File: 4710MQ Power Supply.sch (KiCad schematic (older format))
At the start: 24 parts, among them J1 Jack-DC, J2 ATX 4 Pin, J3 Molex 4 Pin, U1 MP1499GD-Z

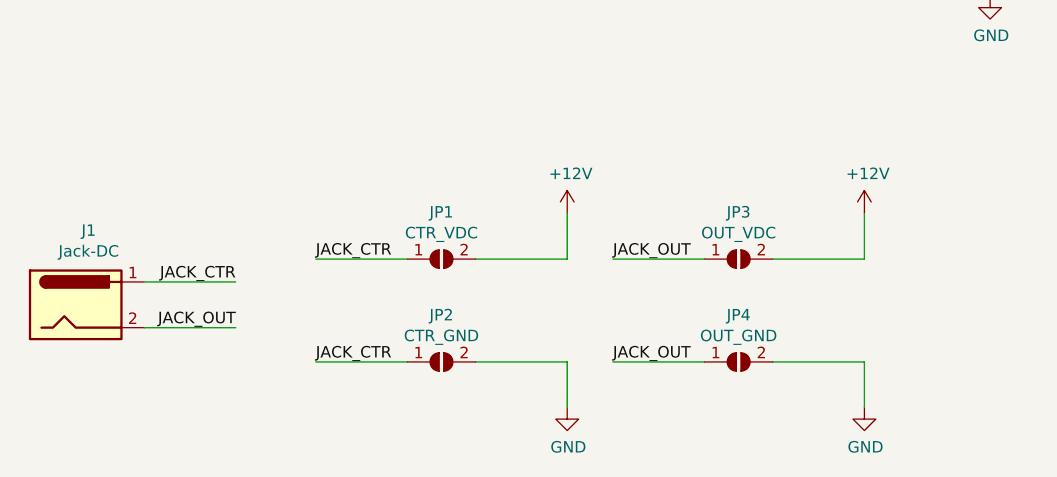
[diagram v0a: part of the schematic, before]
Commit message: Version 1.1
- Add DC-015 (Vertical DC Jack)
- Removed Jumpers (Innerside - +12V / Outside - GND fixed)
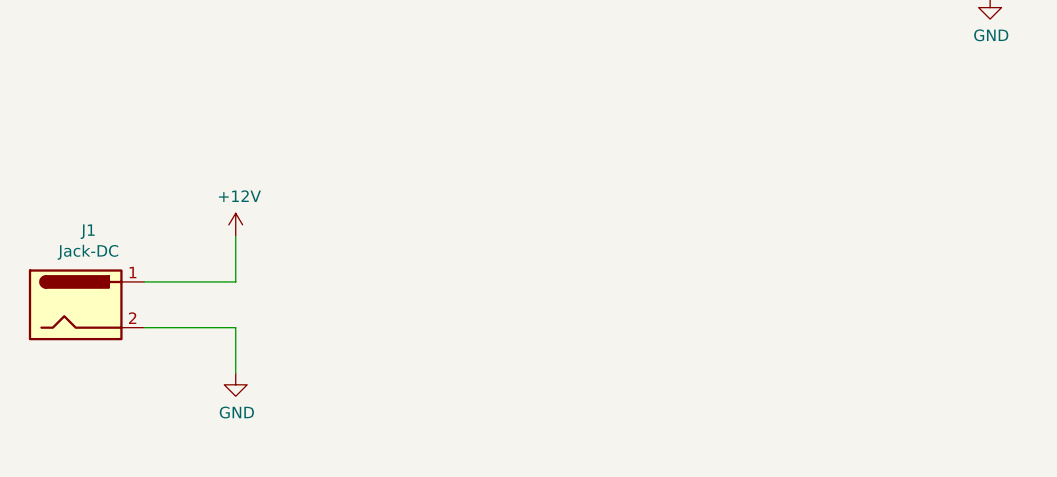
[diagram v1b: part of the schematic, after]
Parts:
- removed JP1: CTR_VDC, Jumper:SolderJumper-3_P1.3mm_Open_Pad1.0x1.5mm_NumberLabels, symbol Jumper:SolderJumper_2_Open
- removed JP2: CTR_GND, Jumper:SolderJumper-3_P1.3mm_Open_Pad1.0x1.5mm_NumberLabels, symbol Jumper:SolderJumper_2_Open
- removed JP3: OUT_VDC, Jumper:SolderJumper-3_P1.3mm_Open_Pad1.0x1.5mm_NumberLabels, symbol Jumper:SolderJumper_2_Open
- removed JP4: OUT_GND, Jumper:SolderJumper-3_P1.3mm_Open_Pad1.0x1.5mm_NumberLabels, symbol Jumper:SolderJumper_2_Open
- J1: footprint Connector_BarrelJack:BarrelJack_CUI_PJ-063AH_Horizontal -> DC015:DC015
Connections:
- net JACK_CTR is gone; now on net +12V: J1.1
- net JACK_OUT is gone; now on net GND: J1.2
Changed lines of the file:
@@
 F 0 "J1" H 907 5425 50  0000 C CNN
 F 1 "Jack-DC" H 907 5334 50  0000 C CNN
-F 2 "Connector_BarrelJack:BarrelJack_CUI_PJ-063AH_Horizontal" H 900 5060 50  0001 C CNN
+F 2 "DC015:DC015" H 900 5060 50  0001 C CNN
 F 3 "~" H 900 5060 50  0001 C CNN
 	1    850  5100
@@
 Wire Wire Line
 	1150 5200 1550 5200
-Text Label 1550 5000 2    50   ~ 0
-JACK_CTR
-Text Label 1550 5200 2    50   ~ 0
-JACK_OUT
-$Comp
-L Jumper:SolderJumper_2_Open JP1
-U 1 1 611D7CEA
-P 2450 4900
-F 0 "JP1" H 2450 5105 50  0000 C CNN
-F 1 "CTR_VDC" H 2450 5014 50  0000 C CNN
-F 2 "Jumper:SolderJumper-3_P1.3mm_Open_Pad1.0x1.5mm_NumberLabels" H 2450 4900 50  0001 C CNN
-F 3 "~" H 2450 4900 50  0001 C CNN
-	1    2450 4900
-	1    0    0    -1
-$EndComp
-Wire Wire Line
-	2300 4900 1900 4900
-Wire Wire Line
-	2600 4900 3000 4900
-Wire Wire Line
-	3000 4900 3000 4700
-$Comp
-L Jumper:SolderJumper_2_Open JP3
-U 1 1 611E0BFC
-P 3750 4900
-F 0 "JP3" H 3750 5105 50  0000 C CNN
-F 1 "OUT_VDC" H 3750 5014 50  0000 C CNN
-F 2 "Jumper:SolderJumper-3_P1.3mm_Open_Pad1.0x1.5mm_NumberLabels" H 3750 4900 50  0001 C CNN
-F 3 "~" H 3750 4900 50  0001 C CNN
-	1    3750 4900
-	1    0    0    -1
-$EndComp
-Wire Wire Line
-	3600 4900 3200 4900
-Wire Wire Line
-	3900 4900 4300 4900
-Wire Wire Line
-	4300 4900 4300 4700
-$Comp
-L Jumper:SolderJumper_2_Open JP2
-U 1 1 611E1F90
-P 2450 5350
-F 0 "JP2" H 2450 5555 50  0000 C CNN
-F 1 "CTR_GND" H 2450 5464 50  0000 C CNN
-F 2 "Jumper:SolderJumper-3_P1.3mm_Open_Pad1.0x1.5mm_NumberLabels" H 2450 5350 50  0001 C CNN
-F 3 "~" H 2450 5350 50  0001 C CNN
-	1    2450 5350
-	1    0    0    -1
-$EndComp
-Wire Wire Line
-	2300 5350 1900 5350
-Wire Wire Line
-	2600 5350 3000 5350
-$Comp
-L Jumper:SolderJumper_2_Open JP4
-U 1 1 611E3280
-P 3750 5350
-F 0 "JP4" H 3750 5555 50  0000 C CNN
-F 1 "OUT_GND" H 3750 5464 50  0000 C CNN
-F 2 "Jumper:SolderJumper-3_P1.3mm_Open_Pad1.0x1.5mm_NumberLabels" H 3750 5350 50  0001 C CNN
-F 3 "~" H 3750 5350 50  0001 C CNN
-	1    3750 5350
-	1    0    0    -1
-$EndComp
-Wire Wire Line
-	3600 5350 3200 5350
-Wire Wire Line
-	3900 5350 4300 5350
-Wire Wire Line
-	3000 5350 3000 5550
-Wire Wire Line
-	4300 5350 4300 5550
-$Comp
-L power:GND #PWR0109
-U 1 1 611E7F6F
-P 3000 5550
-F 0 "#PWR0109" H 3000 5300 50  0001 C CNN
-F 1 "GND" H 3005 5377 50  0000 C CNN
-F 2 "" H 3000 5550 50  0001 C CNN
-F 3 "" H 3000 5550 50  0001 C CNN
-	1    3000 5550
-	1    0    0    -1
-$EndComp
-$Comp
-L power:GND #PWR0110
-U 1 1 611E86F6
-P 4300 5550
-F 0 "#PWR0110" H 4300 5300 50  0001 C CNN
-F 1 "GND" H 4305 5377 50  0000 C CNN
-F 2 "" H 4300 5550 50  0001 C CNN
-F 3 "" H 4300 5550 50  0001 C CNN
-	1    4300 5550
-	1    0    0    -1
-$EndComp
-Text Label 1900 4900 0    50   ~ 0
-JACK_CTR
-Text Label 1900 5350 0    50   ~ 0
-JACK_CTR
-Text Label 3200 4900 0    50   ~ 0
-JACK_OUT
-Text Label 3200 5350 0    50   ~ 0
-JACK_OUT
 Wire Wire Line
 	700  1200 700  1000
@@
 F 3 "" H 6800 1400 50  0001 C CNN
 	1    6800 1400
-	1    0    0    -1
-$EndComp
-$Comp
-L power:+12V #PWR0112
-U 1 1 61204452
-P 4300 4700
-F 0 "#PWR0112" H 4300 4550 50  0001 C CNN
-F 1 "+12V" H 4315 4873 50  0000 C CNN
-F 2 "" H 4300 4700 50  0001 C CNN
-F 3 "" H 4300 4700 50  0001 C CNN
-	1    4300 4700
-	1    0    0    -1
-$EndComp
-$Comp
-L power:+12V #PWR0113
-U 1 1 61204D4E
-P 3000 4700
-F 0 "#PWR0113" H 3000 4550 50  0001 C CNN
-F 1 "+12V" H 3015 4873 50  0000 C CNN
-F 2 "" H 3000 4700 50  0001 C CNN
-F 3 "" H 3000 4700 50  0001 C CNN
-	1    3000 4700
 	1    0    0    -1
 $EndComp
@@
 Wire Wire Line
 	1350 1200 1950 1200
+Wire Wire Line
+	1550 5000 1550 4800
+Wire Wire Line
+	1550 5200 1550 5400
+$Comp
+L power:+12V #PWR0109
+U 1 1 61356D30
+P 1550 4800
+F 0 "#PWR0109" H 1550 4650 50  0001 C CNN
+F 1 "+12V" H 1565 4973 50  0000 C CNN
+F 2 "" H 1550 4800 50  0001 C CNN
+F 3 "" H 1550 4800 50  0001 C CNN
+	1    1550 4800
+	1    0    0    -1
+$EndComp
+$Comp
+L power:GND #PWR0110
+U 1 1 6135740B
+P 1550 5400
+F 0 "#PWR0110" H 1550 5150 50  0001 C CNN
+F 1 "GND" H 1555 5227 50  0000 C CNN
+F 2 "" H 1550 5400 50  0001 C CNN
+F 3 "" H 1550 5400 50  0001 C CNN
+	1    1550 5400
+	1    0    0    -1
+$EndComp
 $EndSCHEMATC

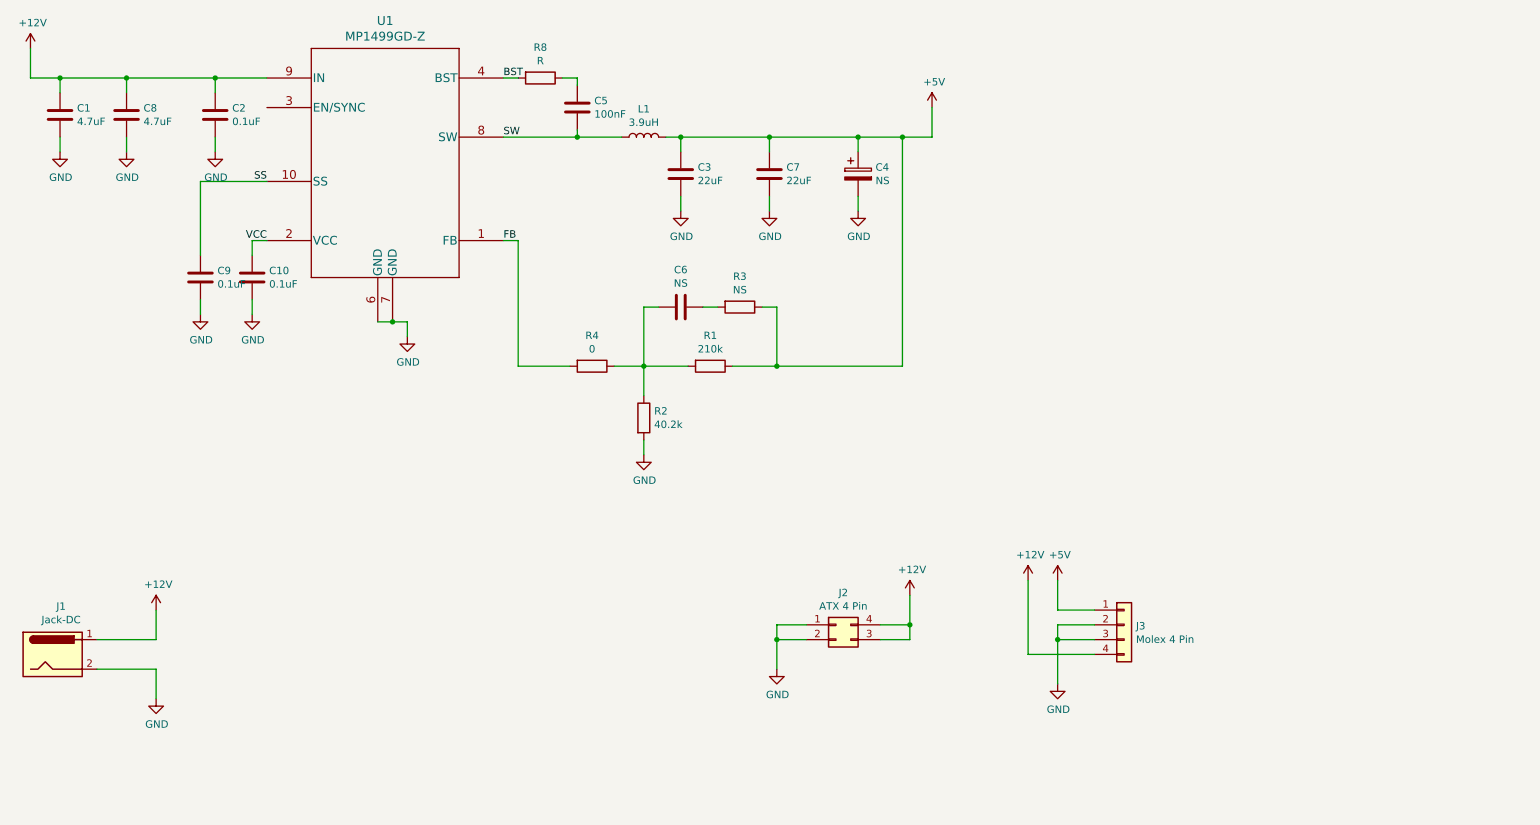
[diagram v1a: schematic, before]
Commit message: [Not Completed] Version 1.2
- 3.3V LDO
- Current Sensor up to 30A
- UART to USB (CH340G)
- ADC 12bit
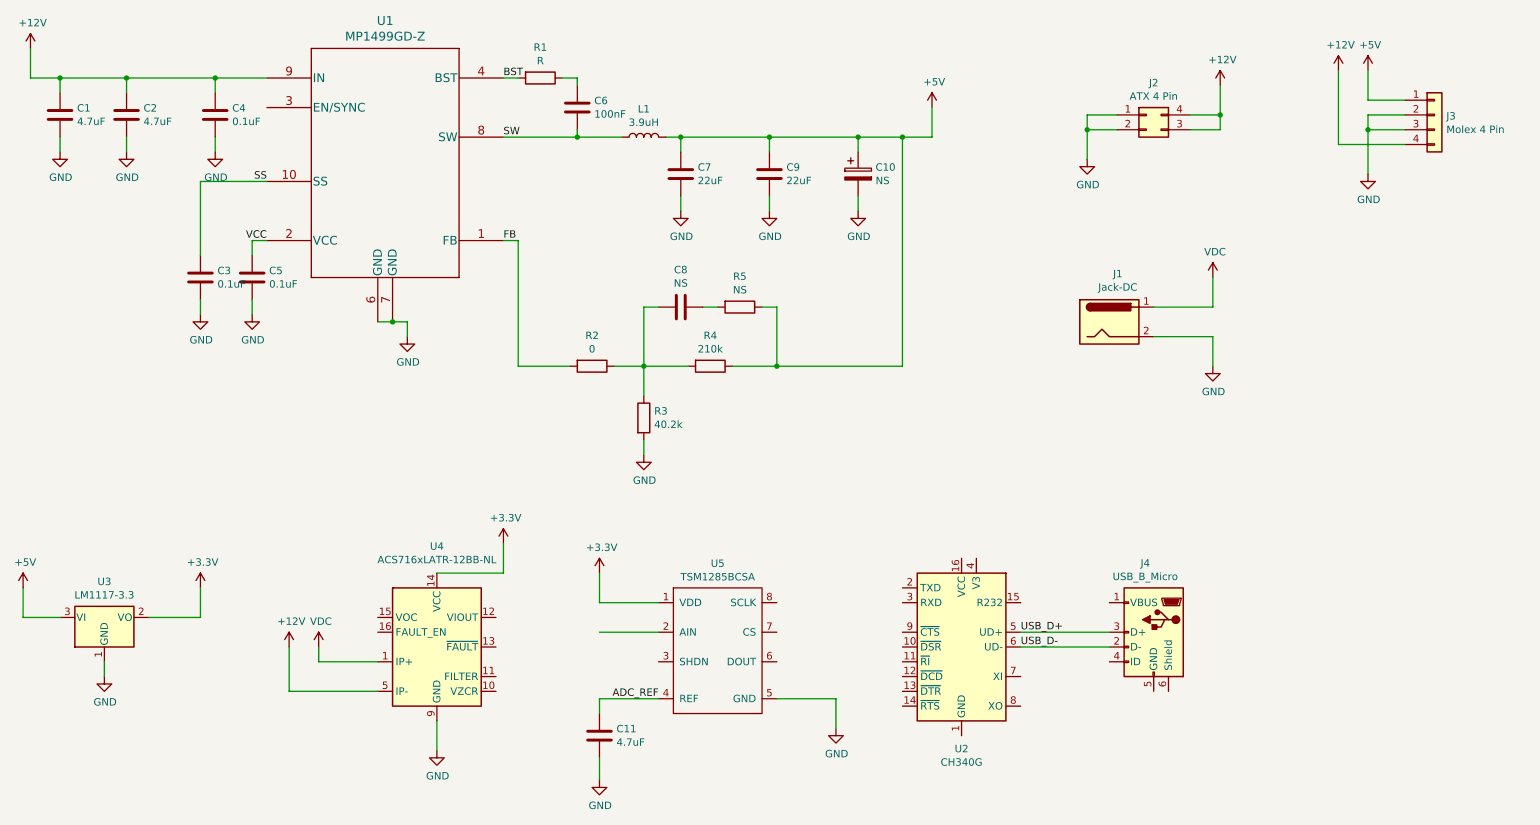
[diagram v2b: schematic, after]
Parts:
- added C11: 4.7uF, Capacitor_SMD:C_1206_3216Metric_Pad1.33x1.80mm_HandSolder, symbol Device:C
- added J4: USB_B_Micro, Connector_USB:USB_Micro-B_Wuerth_614105150721_Vertical, symbol Connector:USB_B_Micro
- added U2: CH340G, Package_SO:SOIC-16_3.9x9.9mm_P1.27mm, symbol Interface_USB:CH340G
- added U3: LM1117-3.3, Package_TO_SOT_SMD:SOT-23_Handsoldering, symbol Regulator_Linear:LM1117-3.3
- added U4: ACS716xLATR-12BB-NL, Package_SO:SOIC-16W_7.5x10.3mm_P1.27mm, symbol Sensor_Current:ACS716xLATR-12BB-NL
- added U5: TSM1285BCSA, Package_SO:SOIC-8_3.9x4.9mm_P1.27mm, symbol TSM1285BCSA:TSM1285BCSA
- renumbered C4 to C10, C8 to C2, C9 to C3, C2 to C4, C10 to C5, C5 to C6, C3 to C7, C6 to C8, C7 to C9, R8 to R1, R4 to R2, R2 to R3, R1 to R4, R3 to R5
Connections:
- net +12V: now also U4.5 (IP-), U4.6 (IP-), U4.7 (IP-), U4.8 (IP-); no longer J1.1
- net +5V: now also U3.3 (VI)
- net GND: now also C11.2, U3.1 (GND), U4.9 (GND), U5.5 (GND)
- new net +3V3: U3.2 (VO), U4.14 (VCC), U5.1 (VDD)
- new net ADC_REF: C11.1, U5.4 (REF)
- new net USB_D+: J4.3 (D+), U2.5 (UD+)
- new net USB_D-: J4.2 (D-), U2.6 (UD-)
- new net VDC: J1.1, U4.1 (IP+), U4.2 (IP+), U4.3 (IP+), U4.4 (IP+)
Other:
- moved on the sheet: J1, J2, J3

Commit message: Version 2.0
- Size Changed
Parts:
- removed C11: 4.7uF, Capacitor_SMD:C_1206_3216Metric_Pad1.33x1.80mm_HandSolder, symbol Device:C
- removed J4: USB_B_Micro, Connector_USB:USB_Micro-B_Wuerth_614105150721_Vertical, symbol Connector:USB_B_Micro
- removed U2: CH340G, Package_SO:SOIC-16_3.9x9.9mm_P1.27mm, symbol Interface_USB:CH340G
- removed U3: LM1117-3.3, Package_TO_SOT_SMD:SOT-23_Handsoldering, symbol Regulator_Linear:LM1117-3.3
- removed U4: ACS716xLATR-12BB-NL, Package_SO:SOIC-16W_7.5x10.3mm_P1.27mm, symbol Sensor_Current:ACS716xLATR-12BB-NL
- removed U5: TSM1285BCSA, Package_SO:SOIC-8_3.9x4.9mm_P1.27mm, symbol TSM1285BCSA:TSM1285BCSA
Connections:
- net VDC is gone; now on net +12V: J1.1
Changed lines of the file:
@@
 Wire Wire Line
 	4850 3650 4850 3750
-$Comp
-L power:GND #PWR010
-U 1 1 611AF7F5
-P 4850 3750
-F 0 "#PWR010" H 4850 3500 50  0001 C CNN
-F 1 "GND" H 4855 3577 50  0000 C CNN
-F 2 "" H 4850 3750 50  0001 C CNN
-F 3 "" H 4850 3750 50  0001 C CNN
-	1    4850 3750
-	1    0    0    -1
-$EndComp
 Wire Wire Line
 	4000 3150 4350 3150
@@
 $EndComp
 $Comp
-L power:VDC #PWR0112
-U 1 1 613D046F
+L power:+12V #PWR0101
+U 1 1 614C8ABC
 P 8700 2550
-F 0 "#PWR0112" H 8700 2450 50  0001 C CNN
-F 1 "VDC" H 8715 2723 50  0000 C CNN
+F 0 "#PWR0101" H 8700 2400 50  0001 C CNN
+F 1 "+12V" H 8715 2723 50  0000 C CNN
 F 2 "" H 8700 2550 50  0001 C CNN
 F 3 "" H 8700 2550 50  0001 C CNN
@@
 	1    0    0    -1
 $EndComp
-Text Label 4950 5400 2    50   ~ 0
-ADC_REF
-Text Label 7400 5050 0    50   ~ 0
-USB_D-
-Text Label 7400 4950 0    50   ~ 0
-USB_D+
-Wire Wire Line
-	7400 5050 8000 5050
-Wire Wire Line
-	7400 4950 8000 4950
-$Comp
-L power:GND #PWR0108
-U 1 1 61468F1F
-P 6150 5600
-F 0 "#PWR0108" H 6150 5350 50  0001 C CNN
-F 1 "GND" H 6155 5427 50  0000 C CNN
-F 2 "" H 6150 5600 50  0001 C CNN
-F 3 "" H 6150 5600 50  0001 C CNN
-	1    6150 5600
-	1    0    0    -1
-$EndComp
-Wire Wire Line
-	6150 5400 6150 5600
-Wire Wire Line
-	5750 5400 6150 5400
-$Comp
-L power:GND #PWR0107
-U 1 1 61465E71
-P 4550 5950
-F 0 "#PWR0107" H 4550 5700 50  0001 C CNN
-F 1 "GND" H 4555 5777 50  0000 C CNN
-F 2 "" H 4550 5950 50  0001 C CNN
-F 3 "" H 4550 5950 50  0001 C CNN
-	1    4550 5950
-	1    0    0    -1
-$EndComp
-Wire Wire Line
-	4550 5800 4550 5950
-$Comp
-L Device:C C11
-U 1 1 61463231
-P 4550 5650
-F 0 "C11" H 4665 5696 50  0000 L CNN
-F 1 "4.7uF" H 4665 5605 50  0000 L CNN
-F 2 "Capacitor_SMD:C_1206_3216Metric_Pad1.33x1.80mm_HandSolder" H 4588 5500 50  0001 C CNN
-F 3 "~" H 4550 5650 50  0001 C CNN
-	1    4550 5650
-	1    0    0    -1
-$EndComp
-Wire Wire Line
-	4550 5400 4550 5500
-Wire Wire Line
-	4950 5400 4550 5400
-Wire Wire Line
-	4950 4950 4550 4950
-$Comp
-L power:+3.3V #PWR0106
-U 1 1 6145DF78
-P 4550 4550
-F 0 "#PWR0106" H 4550 4400 50  0001 C CNN
-F 1 "+3.3V" H 4565 4723 50  0000 C CNN
-F 2 "" H 4550 4550 50  0001 C CNN
-F 3 "" H 4550 4550 50  0001 C CNN
-	1    4550 4550
-	1    0    0    -1
-$EndComp
-Wire Wire Line
-	4550 4750 4550 4550
-Wire Wire Line
-	4950 4750 4550 4750
-$Comp
-L TSM1285BCSA:TSM1285BCSA U5
-U 1 1 61458BA8
-P 5350 5050
-F 0 "U5" H 5350 5615 50  0000 C CNN
-F 1 "TSM1285BCSA" H 5350 5524 50  0000 C CNN
-F 2 "Package_SO:SOIC-8_3.9x4.9mm_P1.27mm" H 5100 5500 50  0001 C CNN
-F 3 "" H 5100 5500 50  0001 C CNN
-	1    5350 5050
-	1    0    0    -1
-$EndComp
-$Comp
-L Connector:USB_B_Micro J4
-U 1 1 614532CD
-P 8300 4950
-F 0 "J4" H 8357 5417 50  0000 C CNN
-F 1 "USB_B_Micro" H 8357 5326 50  0000 C CNN
-F 2 "Connector_USB:USB_Micro-B_Wuerth_614105150721_Vertical" H 8450 4900 50  0001 C CNN
-F 3 "~" H 8450 4900 50  0001 C CNN
-	1    8300 4950
-	-1   0    0    -1
-$EndComp
-$Comp
-L Interface_USB:CH340G U2
-U 1 1 61446B15
-P 7000 5050
-F 0 "U2" H 7000 4361 50  0000 C CNN
-F 1 "CH340G" H 7000 4270 50  0000 C CNN
-F 2 "Package_SO:SOIC-16_3.9x9.9mm_P1.27mm" H 7050 4500 50  0001 L CNN
-F 3 "http://www.datasheet5.com/pdf-local-2195953" H 6650 5850 50  0001 C CNN
-	1    7000 5050
-	-1   0    0    -1
-$EndComp
-$Comp
-L power:GND #PWR0105
-U 1 1 6142B99E
-P 3450 5750
-F 0 "#PWR0105" H 3450 5500 50  0001 C CNN
-F 1 "GND" H 3455 5577 50  0000 C CNN
-F 2 "" H 3450 5750 50  0001 C CNN
-F 3 "" H 3450 5750 50  0001 C CNN
-	1    3450 5750
-	1    0    0    -1
-$EndComp
-Wire Wire Line
-	3450 5550 3450 5750
-$Comp
-L power:+3.3V #PWR0104
-U 1 1 61427B77
-P 3900 4350
-F 0 "#PWR0104" H 3900 4200 50  0001 C CNN
-F 1 "+3.3V" H 3915 4523 50  0000 C CNN
-F 2 "" H 3900 4350 50  0001 C CNN
-F 3 "" H 3900 4350 50  0001 C CNN
-	1    3900 4350
-	1    0    0    -1
-$EndComp
-Wire Wire Line
-	3900 4550 3900 4350
-Wire Wire Line
-	3450 4550 3900 4550
-Wire Wire Line
-	1500 4850 1850 4850
-$Comp
-L power:+3.3V #PWR0103
-U 1 1 6136B787
-P 1850 4650
-F 0 "#PWR0103" H 1850 4500 50  0001 C CNN
-F 1 "+3.3V" H 1865 4823 50  0000 C CNN
-F 2 "" H 1850 4650 50  0001 C CNN
-F 3 "" H 1850 4650 50  0001 C CNN
-	1    1850 4650
-	1    0    0    -1
-$EndComp
-Wire Wire Line
-	1850 4850 1850 4650
-Wire Wire Line
-	2450 5350 3050 5350
-$Comp
-L Sensor_Current:ACS716xLATR-12BB-NL U4
-U 1 1 613E1144
-P 3450 5050
-F 0 "U4" H 3450 5731 50  0000 C CNN
-F 1 "ACS716xLATR-12BB-NL" H 3450 5640 50  0000 C CNN
-F 2 "Package_SO:SOIC-16W_7.5x10.3mm_P1.27mm" H 3800 5000 50  0001 L CIN
-F 3 "http://www.allegromicro.com/~/media/Files/Datasheets/ACS716-Datasheet.ashx?la=en" H 3450 5050 50  0001 C CNN
-	1    3450 5050
-	1    0    0    -1
-$EndComp
-$Comp
-L power:+12V #PWR0114
-U 1 1 613D734C
-P 2450 5050
-F 0 "#PWR0114" H 2450 4900 50  0001 C CNN
-F 1 "+12V" H 2465 5223 50  0000 C CNN
-F 2 "" H 2450 5050 50  0001 C CNN
-F 3 "" H 2450 5050 50  0001 C CNN
-	1    2450 5050
-	1    0    0    -1
-$EndComp
-$Comp
-L power:VDC #PWR0113
-U 1 1 613D6C08
-P 2650 5050
-F 0 "#PWR0113" H 2650 4950 50  0001 C CNN
-F 1 "VDC" H 2665 5223 50  0000 C CNN
-F 2 "" H 2650 5050 50  0001 C CNN
-F 3 "" H 2650 5050 50  0001 C CNN
-	1    2650 5050
-	1    0    0    -1
-$EndComp
-Wire Wire Line
-	2450 5350 2450 5050
-Wire Wire Line
-	2650 5150 2650 5050
-Wire Wire Line
-	3050 5150 2650 5150
-$Comp
-L power:GND #PWR0102
-U 1 1 6136914D
-P 1200 5250
-F 0 "#PWR0102" H 1200 5000 50  0001 C CNN
-F 1 "GND" H 1205 5077 50  0000 C CNN
-F 2 "" H 1200 5250 50  0001 C CNN
-F 3 "" H 1200 5250 50  0001 C CNN
-	1    1200 5250
-	1    0    0    -1
-$EndComp
-$Comp
-L power:+5V #PWR0101
-U 1 1 61368ADC
-P 650 4650
-F 0 "#PWR0101" H 650 4500 50  0001 C CNN
-F 1 "+5V" H 665 4823 50  0000 C CNN
-F 2 "" H 650 4650 50  0001 C CNN
-F 3 "" H 650 4650 50  0001 C CNN
-	1    650  4650
-	1    0    0    -1
-$EndComp
-Wire Wire Line
-	1200 5150 1200 5250
-Wire Wire Line
-	650  4850 650  4650
-Wire Wire Line
-	900  4850 650  4850
-$Comp
-L Regulator_Linear:LM1117-3.3 U3
-U 1 1 61364B65
-P 1200 4850
-F 0 "U3" H 1200 5092 50  0000 C CNN
-F 1 "LM1117-3.3" H 1200 5001 50  0000 C CNN
-F 2 "Package_TO_SOT_SMD:SOT-23_Handsoldering" H 1200 4850 50  0001 C CNN
-F 3 "http://www.ti.com/lit/ds/symlink/lm1117.pdf" H 1200 4850 50  0001 C CNN
-	1    1200 4850
-	1    0    0    -1
-$EndComp
+$Comp
+L power:GND #PWR?
+U 1 1 614CA392
+P 4850 3750
+F 0 "#PWR?" H 4850 3500 50  0001 C CNN
+F 1 "GND" H 4855 3577 50  0000 C CNN
+F 2 "" H 4850 3750 50  0001 C CNN
+F 3 "" H 4850 3750 50  0001 C CNN
+	1    4850 3750
+	1    0    0    -1
+$EndComp
